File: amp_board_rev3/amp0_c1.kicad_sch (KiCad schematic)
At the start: 28 parts, among them U10 SMCJ150A, U7 SMCJ150A, U8 PA343, U9 PA343

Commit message: routing complete
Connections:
- net GND: now also U9.25 (EPAD), U9.26, U9.27
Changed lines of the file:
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@@
 	)
 	(junction
+		(at 182.88 95.25)
+		(diameter 0)
+		(color 0 0 0 0)
+	)
+	(junction
 		(at 219.71 85.09)
 		(diameter 0)
@@
 	(wire
 		(pts
+			(xy 185.42 93.98) (xy 182.88 93.98)
+		)
+		(stroke
+			(width 0)
+			(type default)
+		)
+	)
+	(wire
+		(pts
 			(xy 168.91 128.27) (xy 182.88 128.27)
 		)
@@
 	(wire
 		(pts
+			(xy 182.88 95.25) (xy 182.88 101.6)
+		)
+		(stroke
+			(width 0)
+			(type default)
+		)
+	)
+	(wire
+		(pts
 			(xy 50.8 78.74) (xy 152.4 78.74)
 		)
@@
 	(wire
 		(pts
+			(xy 182.88 93.98) (xy 182.88 95.25)
+		)
+		(stroke
+			(width 0)
+			(type default)
+		)
+	)
+	(wire
+		(pts
 			(xy 335.28 91.44) (xy 336.55 91.44)
 		)
@@
 	(symbol
 		(lib_id "power:GND")
-		(at 182.88 95.25 0)
+		(at 182.88 101.6 0)
 		(unit 1)
 		(exclude_from_sim no)
@@
 		(fields_autoplaced yes)
 		(property "Reference" "#PWR033"
-			(at 182.88 101.6 0)
+			(at 182.88 107.95 0)
 			(effects
 				(font
@@
 		)
 		(property "Value" "GND"
-			(at 182.88 100.33 0)
+			(at 182.88 106.68 0)
 			(effects
 				(font
@@
 		)
 		(property "Footprint" ""
-			(at 182.88 95.25 0)
+			(at 182.88 101.6 0)
 			(effects
 				(font
@@
 		)
 		(property "Datasheet" ""
-			(at 182.88 95.25 0)
+			(at 182.88 101.6 0)
 			(effects
 				(font
@@
 		)
 		(property "Description" "Power symbol creates a global label with name \"GND\" , ground"
-			(at 182.88 95.25 0)
+			(at 182.88 101.6 0)
 			(effects
 				(font

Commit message: all routed
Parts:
- added R42, R44: 10, Resistor_SMD:R_0603_1608Metric, symbol Device:R_US
- added R43, R45: 100, Resistor_SMD:R_0603_1608Metric, symbol Device:R_US
- renumbered C22 to C10, C26 to C14, C19 to C7, C20 to C8, C21 to C9, R14 to R2, R15 to R3, R16 to R4, R17 to R5, R18 to R6, R19 to R7, U7 to U1, U8 to U2, U9 to U3
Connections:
- net GND: now also R43.1, R45.1; no longer C10.2 (-), C14.2 (-), C25.2, C9.2, U1.2 (A), U10.2 (A), U2.12, U2.24, U2.25 (EPAD), U2.26, U2.27, U2.9 (+IN_B), U3.24, U3.25 (EPAD), U3.26, U3.27, U9.12, U9.9 (+IN_B)
- net input_2a_lv: now also R42.1, R43.2; no longer C15.2
- net input_3a_lv: now also R44.1, R45.2; no longer C16.2
- new net: C16.2, R44.2
- new net: C15.2, R42.2
- new net VSS: C10.2 (-), C14.2 (-), C25.2, C9.2, U1.2 (A), U10.2 (A), U2.12, U2.24, U2.25 (EPAD), U2.26, U2.27, U2.9 (+IN_B), U3.24, U3.25 (EPAD), U3.26, U3.27, U9.12, U9.9 (+IN_B)

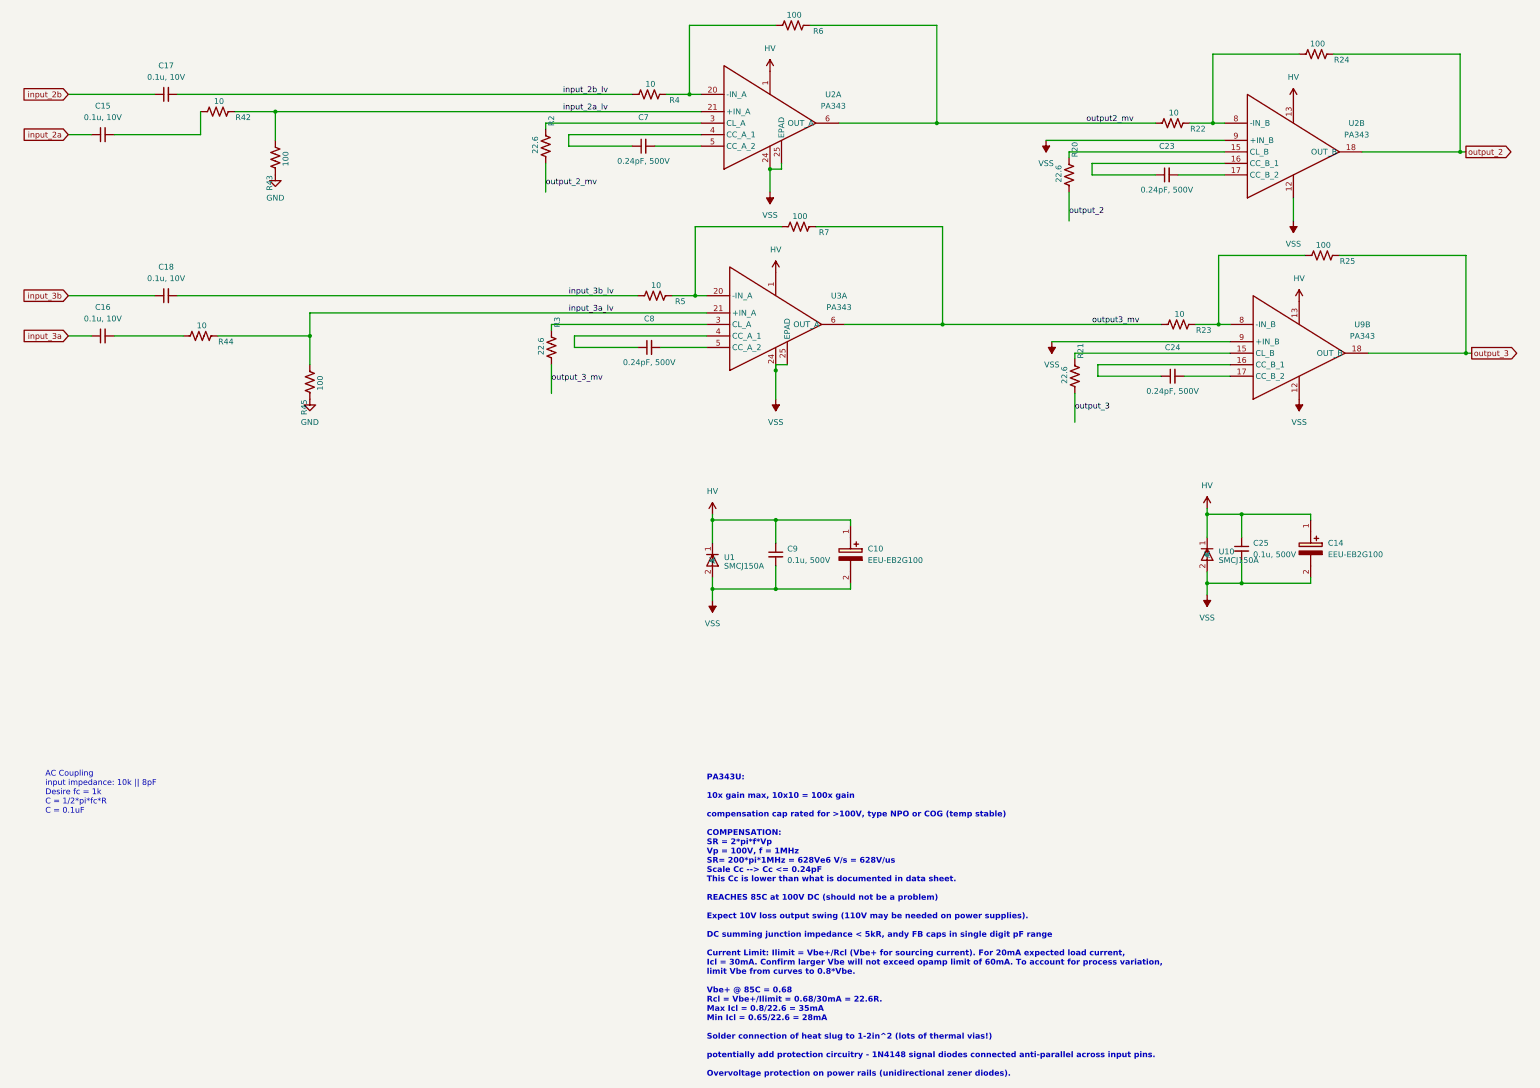
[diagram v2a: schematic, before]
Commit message: updated ground references in schematic
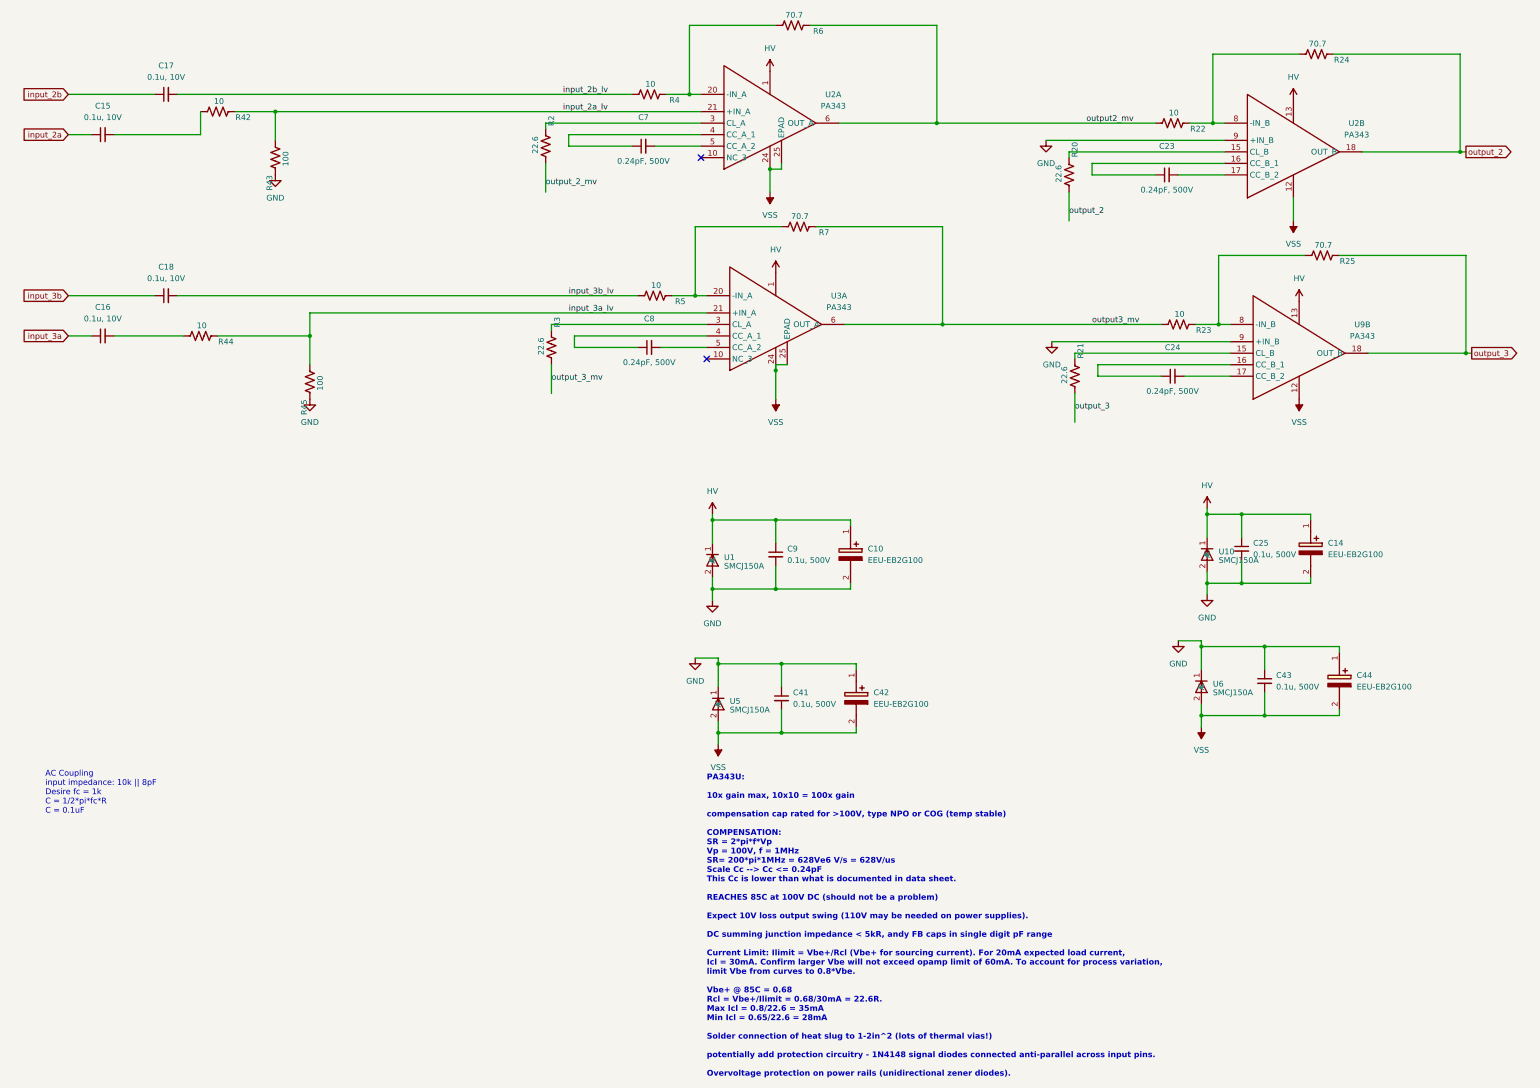
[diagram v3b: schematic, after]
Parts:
- added C41, C43: 0.1u, 500V, Capacitor_SMD:C_1812_4532Metric, symbol Device:C_Small
- added C42, C44: EEU-EB2G100, 726_footprints:EEU-EB2G100, symbol _PHASE:EEU-EB2G100
- added U5, U6: SMCJ150A, 726_footprints:SMCJ150A-13-F, symbol _PHASE:SMCJ150A-13-F
- R24, R25, R6, R7: value 100 -> 70.7
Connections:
- net GND: now also C10.2 (-), C14.2 (-), C25.2, C9.2, U1.2 (A), U10.2 (A), U2.9 (+IN_B), U9.9 (+IN_B), C41.1, C42.1 (+), C43.1, C44.1 (+), U5.1 (K), U6.1 (K)
- net VSS: now also C41.2, C42.2 (-), C43.2, C44.2 (-), U5.2 (A), U6.2 (A); no longer C10.2 (-), C14.2 (-), C25.2, C9.2, U1.2 (A), U10.2 (A), U2.9 (+IN_B), U9.9 (+IN_B)
- no-connect marks 0 -> 2

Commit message: updates based on 11/14 meeting
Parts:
- C10, C14, C42, C44: footprint 726_footprints:EEU-EB2G100 -> CAPPRD500W65D1000H2200
- C15, C16, C17, C18: footprint Capacitor_SMD:C_0603_1608Metric -> (none)
- C23, C24: value 0.24pF, 500V -> 0.2pF, 250V; footprint Capacitor_SMD:C_0402_1005Metric -> (none)
- C25, C41, C43, C9: footprint Capacitor_SMD:C_1812_4532Metric -> (none)
- C7, C8: value 0.24pF, 500V -> 0.75pF, 250V; footprint Capacitor_SMD:C_0402_1005Metric -> (none)
- R2, R20, R21, R22, R23, R24, R25, R3, R4, R42, R43, R44, R45, R5, R6, R7: footprint Resistor_SMD:R_0603_1608Metric -> (none)
- U2, U3: footprint 726_footprints:PA341DF -> (none)
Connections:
- now unconnected: U2.10 (NC_3), U2.11 (NC_4), U2.14 (NC_5), U2.7 (NC_2), U3.10 (NC_3), U3.11 (NC_4), U3.14 (NC_5), U3.7 (NC_2)
